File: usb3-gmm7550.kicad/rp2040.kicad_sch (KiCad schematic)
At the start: 54 parts

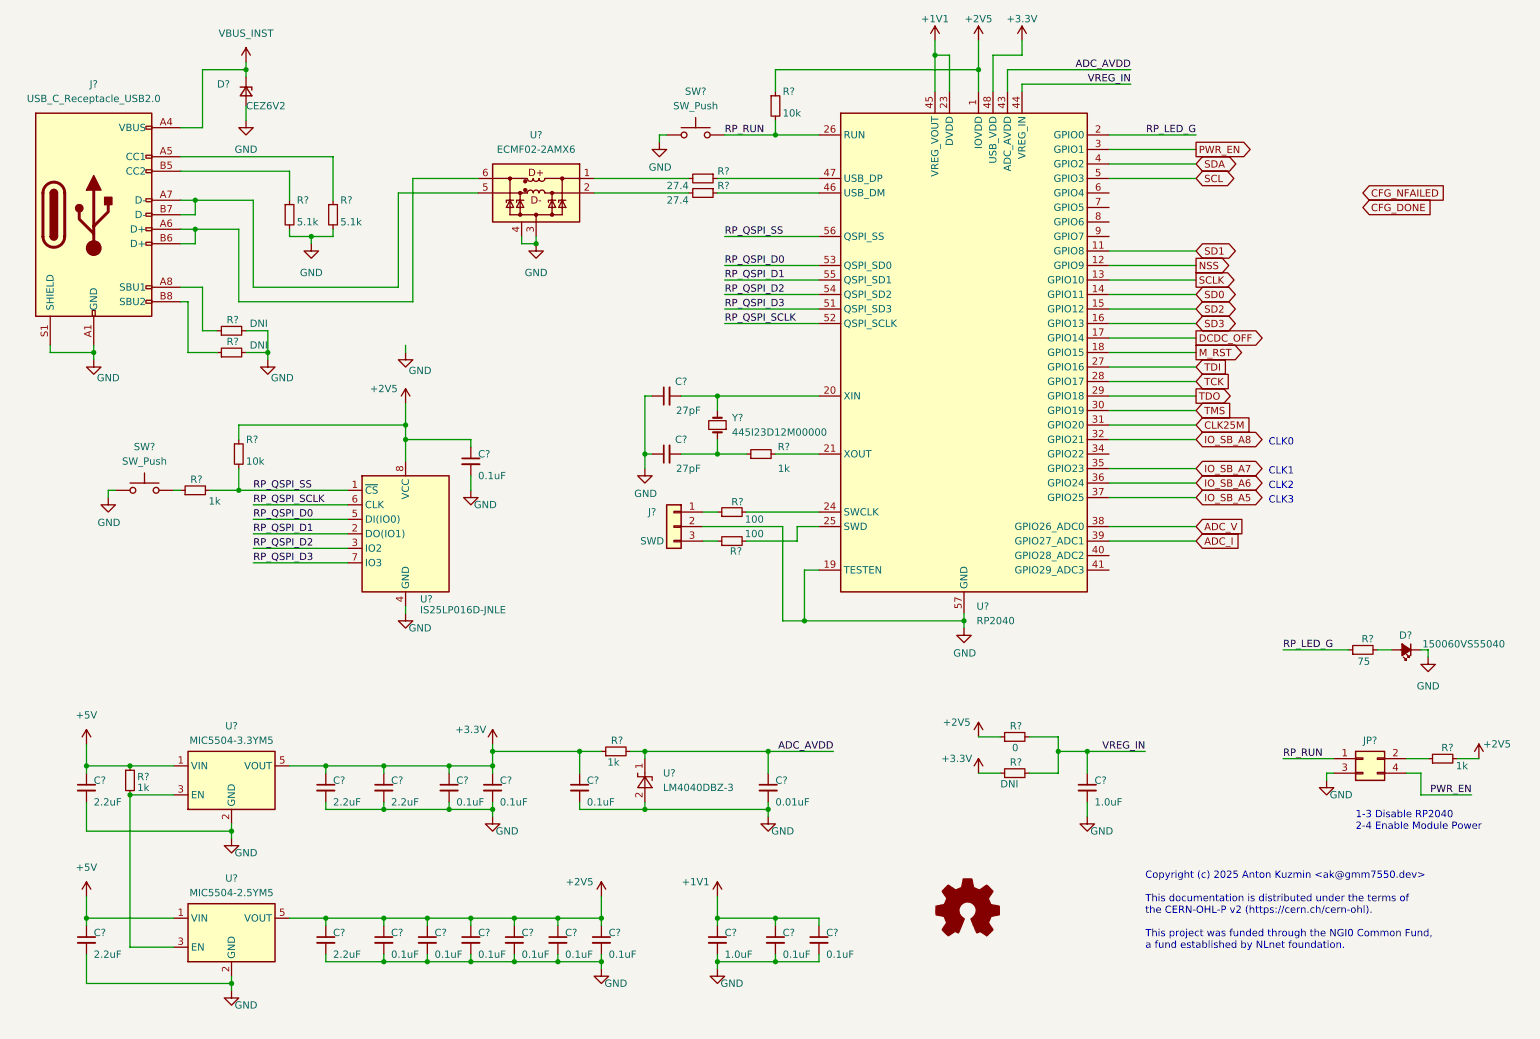
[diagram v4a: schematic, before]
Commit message: USB 3 adapter schematic: revision 0.9 (pre-layout) is ready
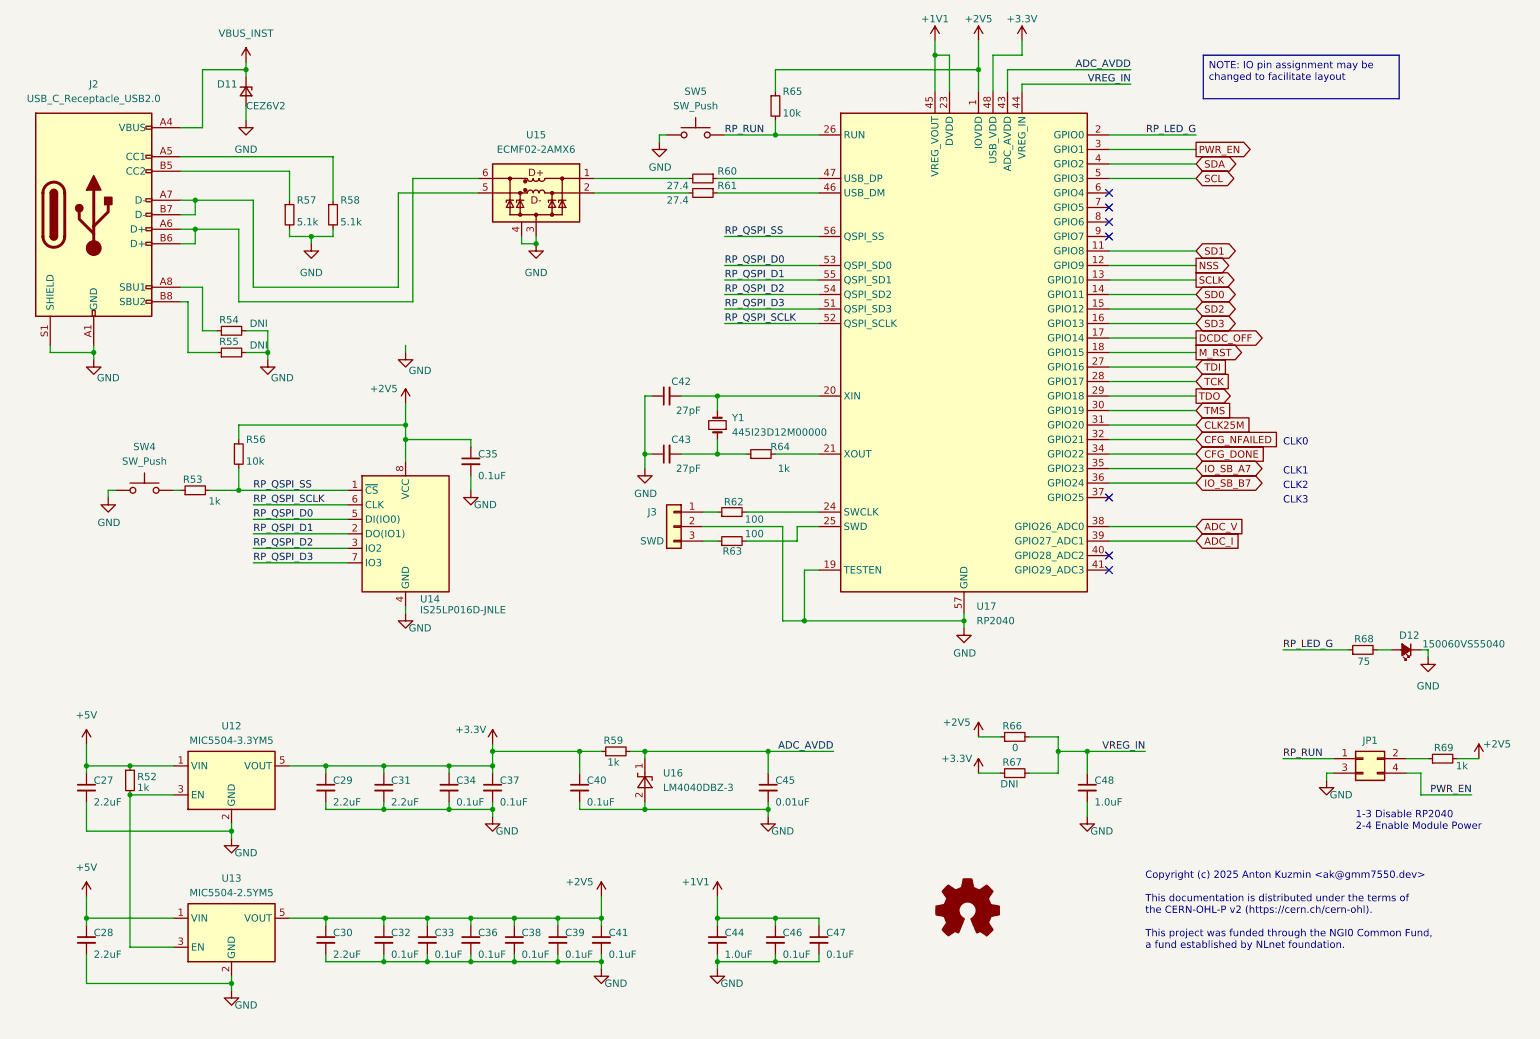
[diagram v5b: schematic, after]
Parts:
- gave numbers to parts that had none: 54
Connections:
- net IO_SB_A8 is gone; now on net CFG_NFAILED: U17.32 (GPIO21)
- net CFG_DONE: now also U17.34 (GPIO22)
- net IO_SB_A5: no longer names the net of U17.37 (GPIO25)
- net IO_SB_A6 renamed IO_SB_B7
- no-connect marks 0 -> 7

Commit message: Placement: WIP, schematic update to 0.9.1 -- BoM simplification and minor improvements
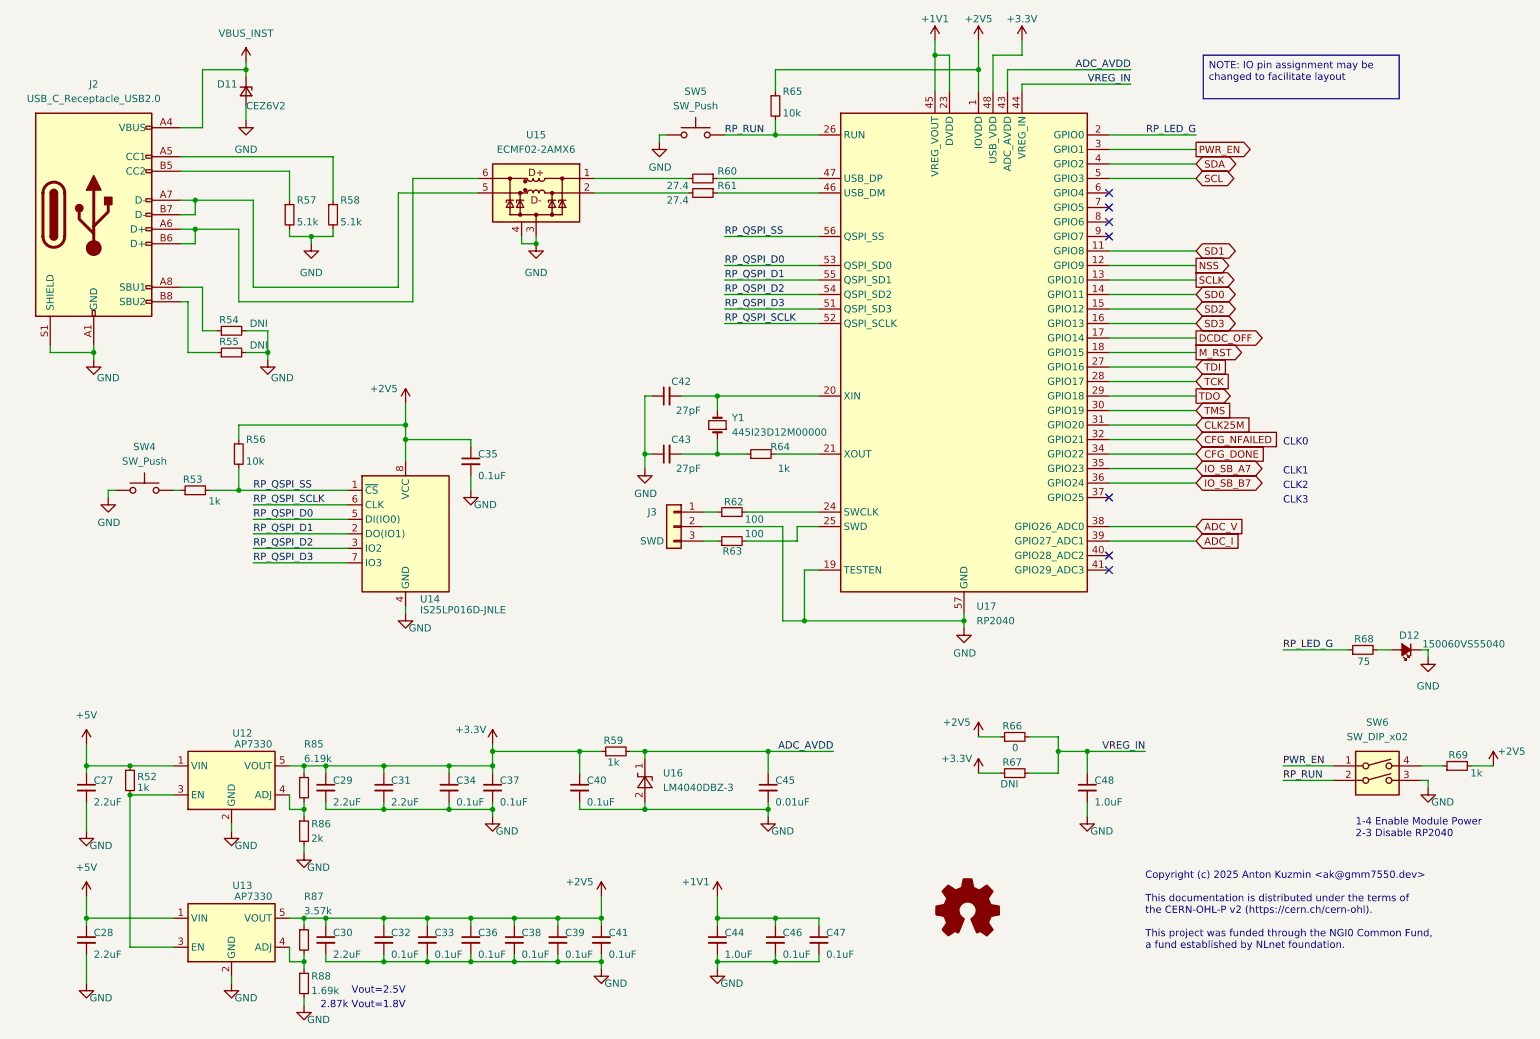
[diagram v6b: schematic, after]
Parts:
- removed JP1: Conn_02x02_Odd_Even, Connector_PinHeader_2.54mm:PinHeader_2x02_P2.54mm_Vertical, symbol Connector_Generic:Conn_02x02_Odd_Even
- removed U12: MIC5504-3.3YM5, Package_TO_SOT_SMD:SOT-23-5, symbol Regulator_Linear:MIC5504-3.3YM5
- removed U13: MIC5504-2.5YM5, Package_TO_SOT_SMD:SOT-23-5, symbol Regulator_Linear:MIC5504-2.5YM5
- added R85: 6.19k, Resistor_SMD:R_0402_1005Metric, symbol Device:R_Small
- added R86: 2k, Resistor_SMD:R_0402_1005Metric, symbol Device:R_Small
- added R87: 3.57k, Resistor_SMD:R_0402_1005Metric, symbol Device:R_Small
- added R88: 1.69k, Resistor_SMD:R_0402_1005Metric, symbol Device:R_Small
- added SW6: SW_DIP_x02, Button_Switch_SMD:SW_DIP_SPSTx02_Slide_Omron_A6H-2101_W6.15mm_P1.27mm, symbol Switch:SW_DIP_x02
- added U12, U13: AP7330, Package_TO_SOT_SMD:SOT-23-5, symbol usb3-gmm7550:AP7330
- SW4, SW5: footprint pts810:SW_SPST_PTS810 -> Button_Switch_SMD:SW_SPST_PTS810
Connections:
- net +2V5: now also R87.1, U13.5 (VOUT)
- net +3.3V: now also R85.1, U12.5 (VOUT)
- net +5V: now also U12.1 (VIN), U13.1 (VIN)
- net GND: now also R86.2, R88.2, SW6.3, U12.2 (GND), U13.2 (GND)
- net PWR_EN: now also SW6.1
- net RP_RUN: now also SW6.2
- net at R69.1: now also SW6.4
- net at R52.2: now also U12.3 (EN), U13.3 (EN)
- new net: R87.2, R88.1, U13.4 (ADJ)
- new net: R85.2, R86.1, U12.4 (ADJ)
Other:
- note added: "1-4 Enable Module Power 2-3 Disable RP2040"
- note added: "2.87k Vout=1.8V"
- note added: "Vout=2.5V"
- note removed: "1-3 Disable RP2040 2-4 Enable Module Power"
- moved on the sheet: R69

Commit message: Change to smaller resistors
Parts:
- R68: footprint Resistor_SMD:R_0603_1608Metric -> Resistor_SMD:R_0402_1005Metric
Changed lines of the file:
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@@
 			)
 		)
-		(property "Footprint" "Resistor_SMD:R_0603_1608Metric"
+		(property "Footprint" "Resistor_SMD:R_0402_1005Metric"
 			(at 252.73 128.27 0)
 			(effects

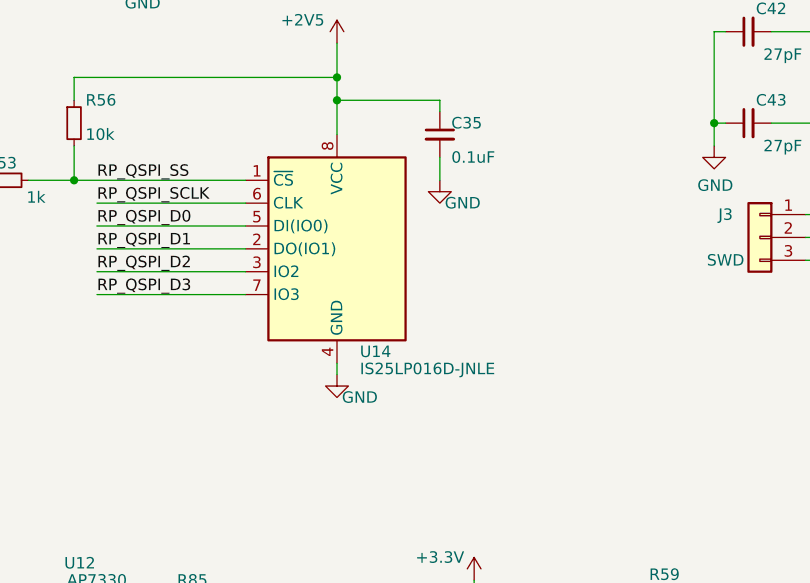
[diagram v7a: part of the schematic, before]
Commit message: Change SPI NOR Flash (U14) to smaller package and wide Vcc range (for possible update to Vio=1.8V)
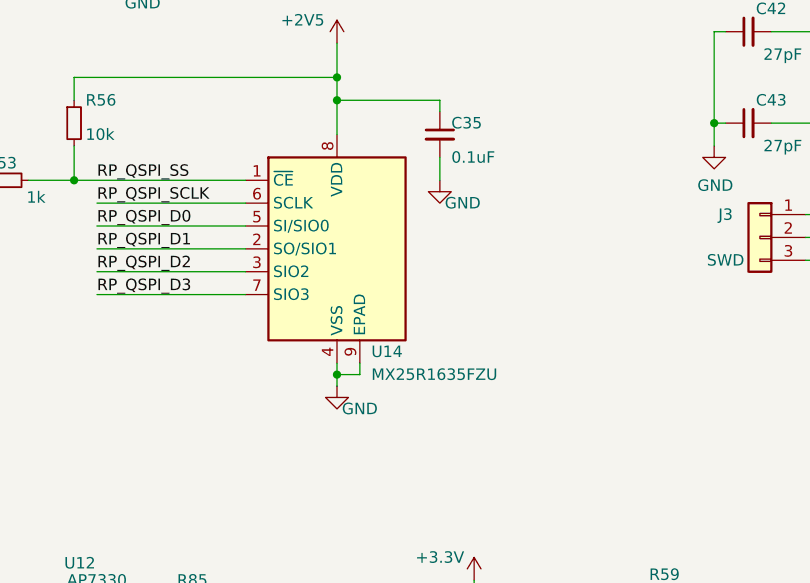
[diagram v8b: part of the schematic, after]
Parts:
- removed U14: IS25LP016D-JNLE, Package_SO:SOIC-8_3.9x4.9mm_P1.27mm, symbol Memory_Flash:W25Q32JVSS
- added U14: MX25R1635FZU, Package_SON:Winbond_USON-8-1EP_3x2mm_P0.5mm_EP0.2x1.6mm, symbol usb3-gmm7550:MX25R1635FZU
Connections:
- net +2V5: now also U14.8 (VDD)
- net GND: now also U14.4 (VSS), U14.9 (EPAD)
- net RP_QSPI_D0: now also U14.5 (SI/SIO0)
- net RP_QSPI_D1: now also U14.2 (SO/SIO1)
- net RP_QSPI_D2: now also U14.3 (SIO2)
- net RP_QSPI_D3: now also U14.7 (SIO3)
- net RP_QSPI_SCLK: now also U14.6 (SCLK)
- net RP_QSPI_SS: now also U14.1 (~{CE})
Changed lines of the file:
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@@
 	)
 	(junction
+		(at 85.09 121.92)
+		(diameter 0)
+		(color 0 0 0 0)
+	)
+	(junction
 		(at 104.14 175.26)
 		(diameter 0)
@@
 	(wire
 		(pts
+			(xy 87.63 120.65) (xy 87.63 121.92)
+		)
+		(stroke
+			(width 0)
+			(type default)
+		)
+	)
+	(wire
+		(pts
 			(xy 151.13 123.19) (xy 154.94 123.19)
 		)
@@
 	(wire
 		(pts
+			(xy 85.09 121.92) (xy 85.09 123.19)
+		)
+		(stroke
+			(width 0)
+			(type default)
+		)
+	)
+	(wire
+		(pts
 			(xy 92.71 156.21) (xy 100.33 156.21)
 		)
@@
 	(wire
 		(pts
+			(xy 87.63 121.92) (xy 85.09 121.92)
+		)
+		(stroke
+			(width 0)
+			(type default)
+		)
+	)
+	(wire
+		(pts
 			(xy 139.7 182.88) (xy 149.86 182.88)
 		)
@@
 	)
 	(symbol
+		(lib_id "usb3-gmm7550:MX25R1635FZU")
+		(at 85.09 107.95 0)
+		(unit 1)
+		(exclude_from_sim no)
+		(in_bom yes)
+		(on_board yes)
+		(dnp no)
+		(property "Reference" "U14"
+			(at 88.9 119.38 0)
+			(effects
+				(font
+					(size 1.27 1.27)
+				)
+				(justify left)
+			)
+		)
+		(property "Value" "MX25R1635FZU"
+			(at 88.9 121.92 0)
+			(effects
+				(font
+					(size 1.27 1.27)
+				)
+				(justify left)
+			)
+		)
+		(property "Footprint" "Package_SON:Winbond_USON-8-1EP_3x2mm_P0.5mm_EP0.2x1.6mm"
+			(at 85.09 123.19 0)
+			(effects
+				(font
+					(size 1.27 1.27)
+				)
+				(hide yes)
+			)
+		)
+		(property "Datasheet" "https://www.mouser.com/datasheet/2/1127/APM_PSRAM_QSPI_APS1604M_SQR_v2_5_PKG-1954861.pdf"
+			(at 85.09 125.73 0)
+			(effects
+				(font
+					(size 1.27 1.27)
+				)
+				(hide yes)
+			)
+		)
+		(property "Description" "16 Mbit [x1/x2/x4] Serial Multi-I/O Flash Memory, 1.65-3.6V, USON-8 3x2mm"
+			(at 85.09 128.27 0)
+			(effects
+				(font
+					(size 1.27 1.27)
+				)
+				(hide yes)
+			)
+		)
+		(pin "9"
+		)
+		(pin "3"
+		)
+		(pin "7"
+		)
+		(pin "8"
+		)
+		(pin "1"
+		)
+		(pin "2"
+		)
+		(pin "5"
+		)
+		(pin "6"
+		)
+		(pin "4"
+		)
+		(instances
+			(project ""
+				(path "/e63e39d7-6ac0-4ffd-8aa3-1841a4541b55/e61e69ec-0946-4002-8138-f431262732c1"
+					(reference "U14")
+					(unit 1)
+				)
+			)
+		)
+	)
+	(symbol
 		(lib_id "power:GND")
 		(at 54.61 160.02 0)
@@
 	)
 	(symbol
-		(lib_id "Memory_Flash:W25Q32JVSS")
-		(at 85.09 107.95 0)
-		(unit 1)
-		(exclude_from_sim no)
-		(in_bom yes)
-		(on_board yes)
-		(dnp no)
-		(property "Reference" "U14"
-			(at 87.63 119.38 0)
-			(effects
-				(font
-					(size 1.27 1.27)
-				)
-				(justify left)
-			)
-		)
-		(property "Value" "IS25LP016D-JNLE"
-			(at 87.63 121.285 0)
-			(effects
-				(font
-					(size 1.27 1.27)
-				)
-				(justify left)
-			)
-		)
-		(property "Footprint" "Package_SO:SOIC-8_3.9x4.9mm_P1.27mm"
-			(at 85.09 107.95 0)
-			(effects
-				(font
-					(size 1.27 1.27)
-				)
-				(hide yes)
-			)
-		)
-		(property "Datasheet" "http://www.winbond.com/resource-files/w25q32jv%20revg%2003272018%20plus.pdf"
-			(at 85.09 107.95 0)
-			(effects
-				(font
-					(size 1.27 1.27)
-				)
-				(hide yes)
-			)
-		)
-		(property "Description" ""
-			(at 85.09 107.95 0)
-			(effects
-				(font
-					(size 1.27 1.27)
-				)
-				(hide yes)
-			)
-		)
-		(pin "2"
-		)
-		(pin "8"
-		)
-		(pin "6"
-		)
-		(pin "1"
-		)
-		(pin "3"
-		)
-		(pin "5"
-		)
-		(pin "4"
-		)
-		(pin "7"
-		)
-		(instances
-			(project "usb-gmm7550"
-				(path "/e63e39d7-6ac0-4ffd-8aa3-1841a4541b55/e61e69ec-0946-4002-8138-f431262732c1"
-					(reference "U14")
-					(unit 1)
-				)
-			)
-		)
-	)
-	(symbol
 		(lib_id "Device:C_Small")
 		(at 115.57 152.4 0)
@@
 	(symbol
 		(lib_id "power:GND")
-		(at 85.09 121.92 0)
+		(at 85.09 123.19 0)
 		(unit 1)
 		(exclude_from_sim no)
@@
 		(dnp no)
 		(property "Reference" "#PWR076"
-			(at 85.09 128.27 0)
+			(at 85.09 129.54 0)
 			(effects
 				(font
@@
 		)
 		(property "Value" "GND"
-			(at 87.63 124.46 0)
+			(at 87.63 125.73 0)
 			(effects
 				(font
@@
 		)
 		(property "Footprint" ""
-			(at 85.09 121.92 0)
+			(at 85.09 123.19 0)
 			(effects
 				(font
@@
 		)
 		(property "Datasheet" ""
-			(at 85.09 121.92 0)
+			(at 85.09 123.19 0)
 			(effects
 				(font
@@
 		)
 		(property "Description" ""
-			(at 85.09 121.92 0)
+			(at 85.09 123.19 0)
 			(effects
 				(font
